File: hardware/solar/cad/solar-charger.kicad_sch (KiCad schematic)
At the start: 20 parts, among them J1 ISENSE_SOLAR, J2 Conn_01x02_Male, J3 ISENSE_DISCHARGE, J4 Conn_01x02_Male, Q1 AOI21357, Q2 AOI21357, Q3 AOI21357, Q4 AOI21357

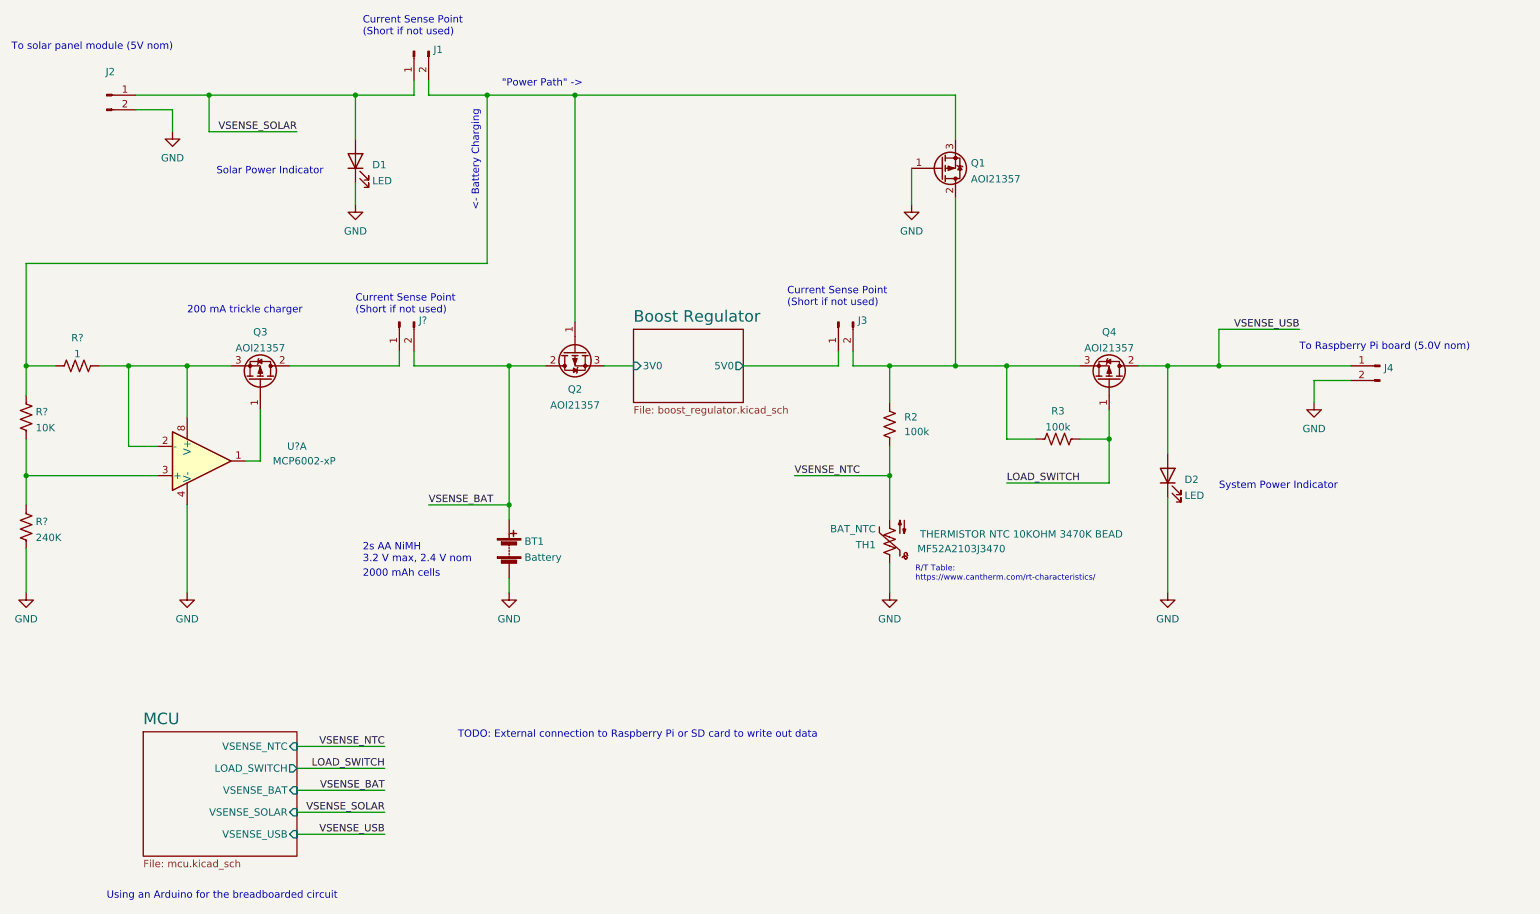
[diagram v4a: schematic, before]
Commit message: Add external I2C connection, LED resistors, op-amp power connections
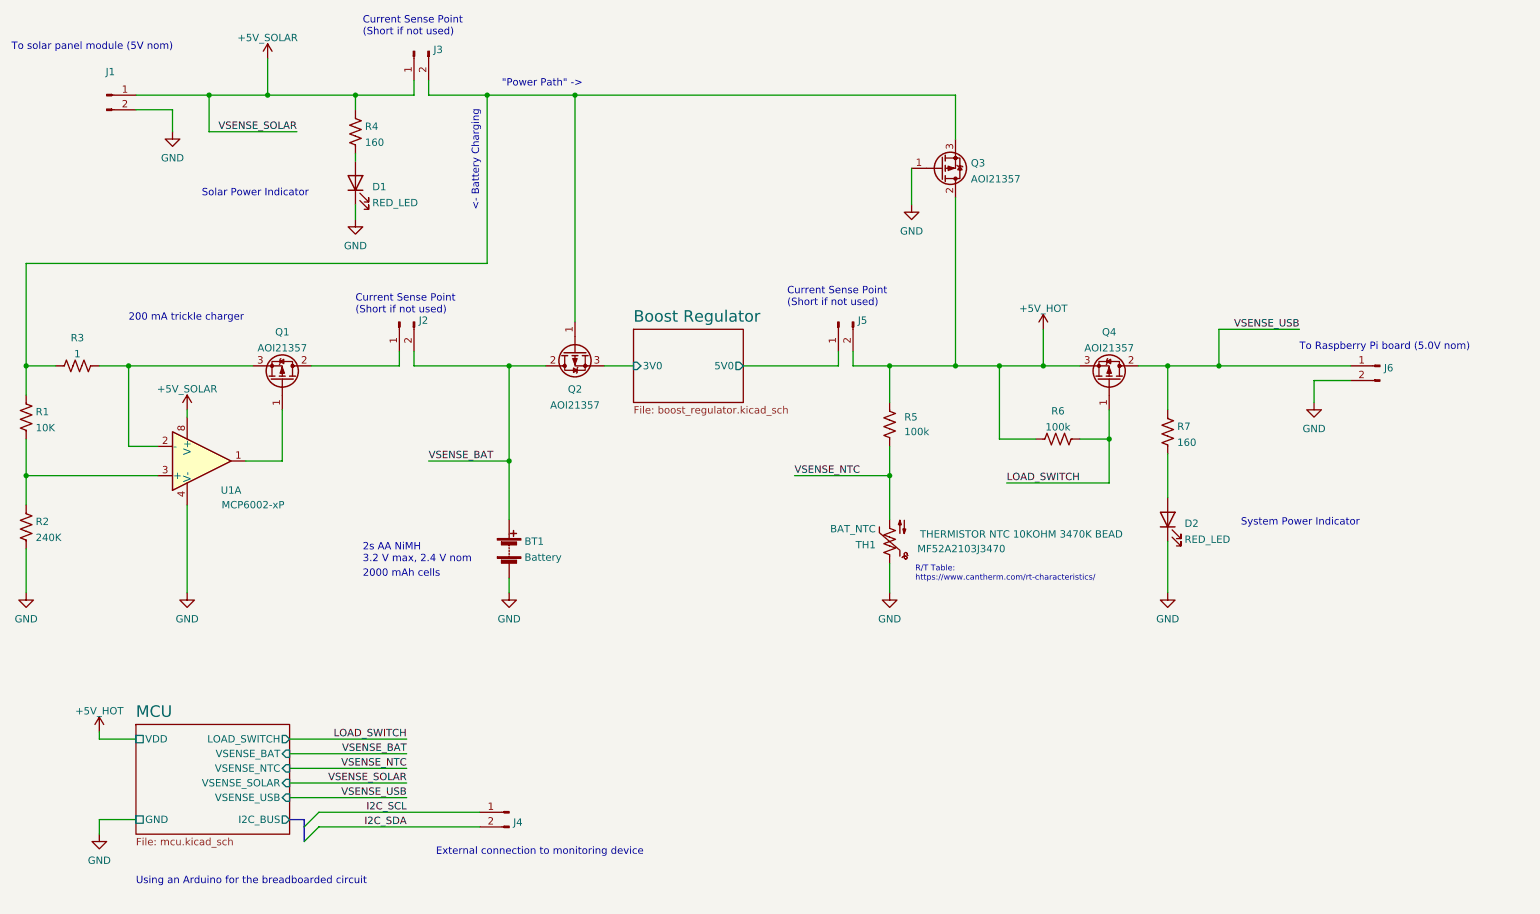
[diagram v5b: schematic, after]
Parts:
- added J4: ISENSE_SOLAR, symbol Connector:Conn_01x02_Male
- added R4, R7: 160, symbol Device:R_US
- D1, D2: value LED -> RED_LED
- gave numbers to parts that had none: 5
- renumbered J2 to J1, J1 to J3, J3 to J5, J4 to J6, Q3 to Q1, Q1 to Q3, R2 to R5, R3 to R6
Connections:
- net VSENSE_USB: now also R7.1; no longer D2.2 (A)
- net at Q1.3 (S), R3.2, U1.2 (-): no longer U1.8 (V+)
- net +5V: now reaches J5.2 (Pin_2), Q3.2 (D), Q4.3 (S), R5.1, R6.1
- net +5V: now also J1.1 (Pin_1), J3.1 (Pin_1), U1.8 (V+), R4.1
- removed net VSENSE_SOLAR: D1.2 (A), J1.1 (Pin_1), J3.1 (Pin_1)
- new net: D1.2 (A), R4.2
- new net: D2.2 (A), R7.2
- new net I2C_SCL: J4.1 (Pin_1)
- new net I2C_SDA: J4.2 (Pin_2)
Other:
- sheet MCU ports: added GND, I2C_BUS, VDD; removed none
- note added: "External connection to monitoring device"
- note removed: "TODO: External connection to Raspberry Pi or SD card to write out data"
- moved on the sheet: D1, D2, Q1

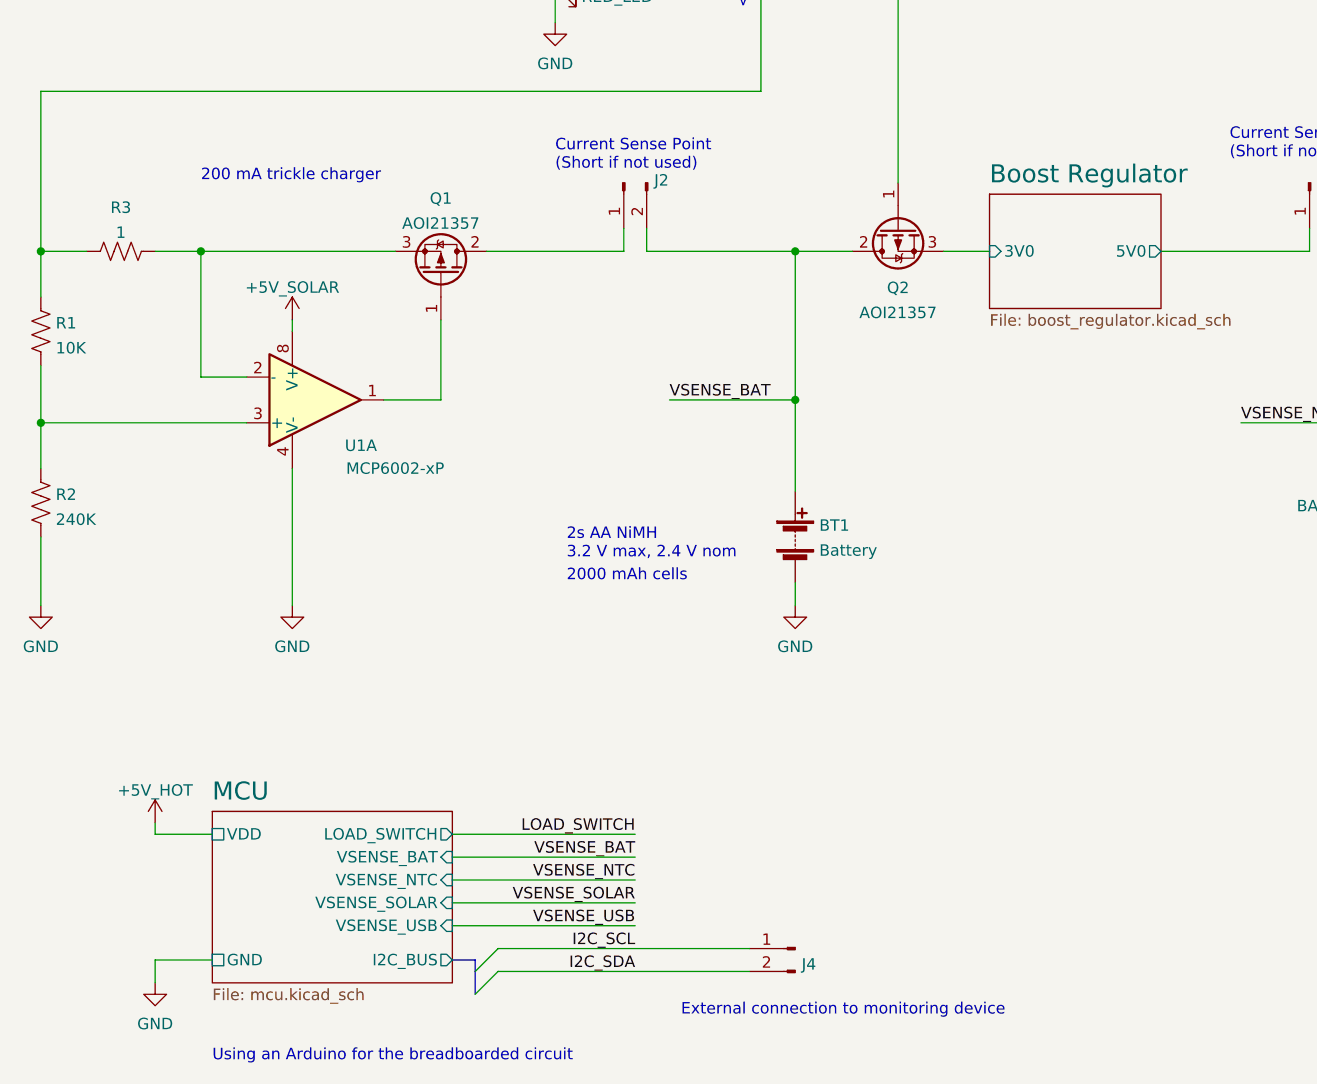
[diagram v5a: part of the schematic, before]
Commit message: add RTC, change charge current based on revised capacity of 1300mAh
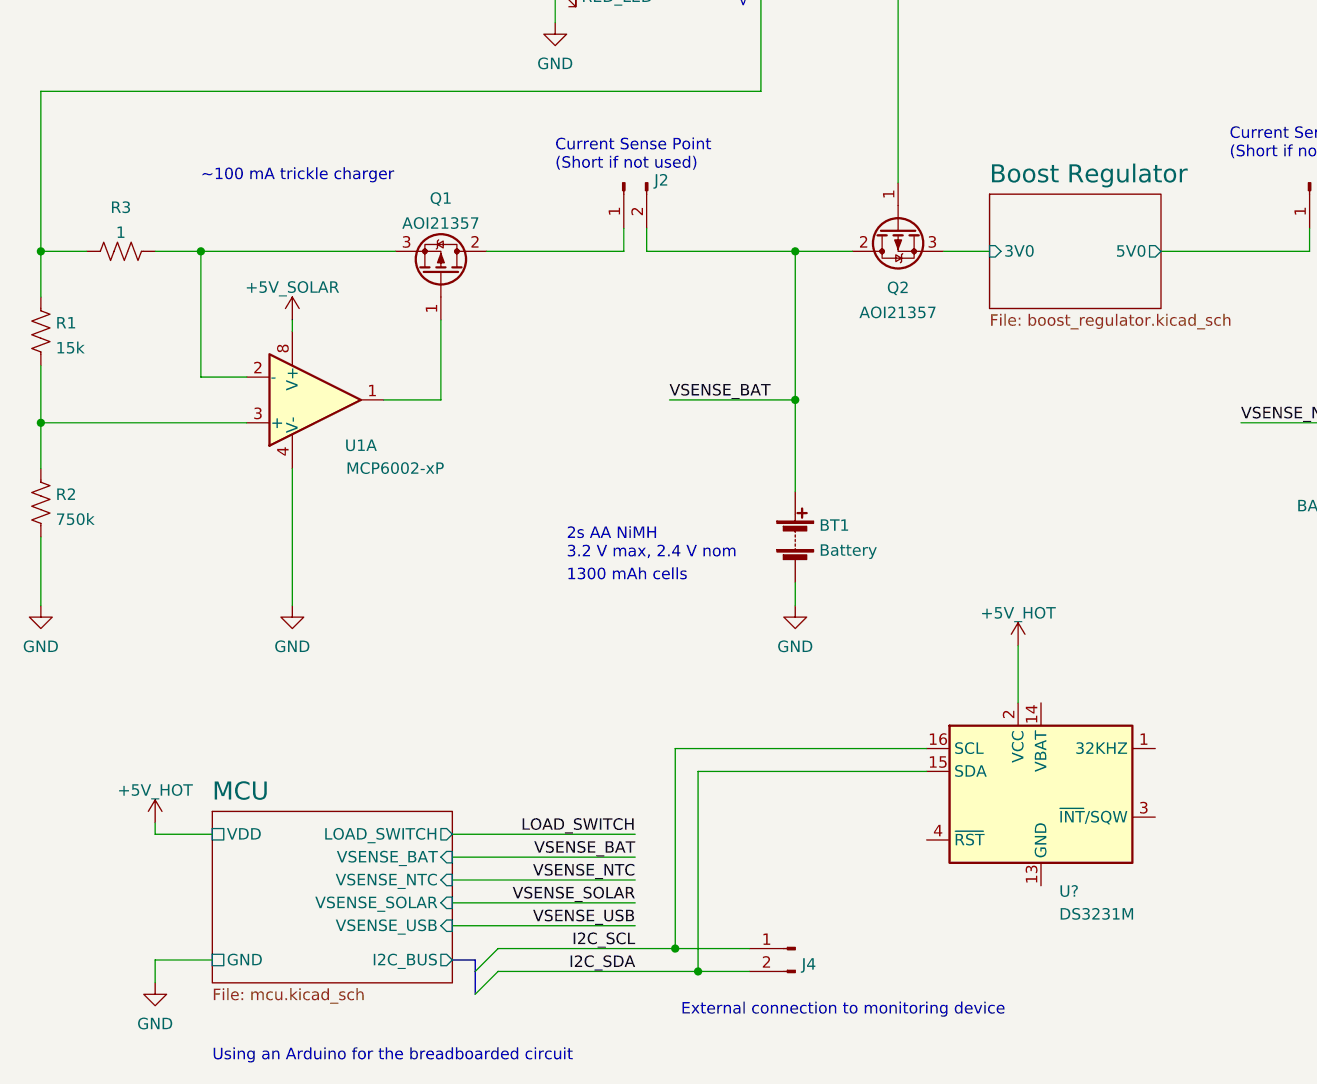
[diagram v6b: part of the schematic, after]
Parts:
- added U?: DS3231M, Package_SO:SOIC-16W_7.5x10.3mm_P1.27mm, symbol Timer_RTC:DS3231M
- R1: value 10K -> 15k
- R2: value 240K -> 750k
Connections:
- net +5V: now also U?.2 (VCC)
- net I2C_SCL: now also U?.16 (SCL)
- net I2C_SDA: now also U?.15 (SDA)
- new net: U?.10 (GND), U?.11 (GND), U?.12 (GND), U?.13 (GND), U?.5 (GND), U?.6 (GND), U?.7 (GND), U?.8 (GND), U?.9 (GND)
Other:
- note added: "1300 mAh cells"
- note added: "~100 mA trickle charger"
- note removed: "200 mA trickle charger"
- note removed: "2000 mAh cells"
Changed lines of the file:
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@@
   (junction (at 232.41 92.71) (diameter 0) (color 0 0 0 0)
   )
+  (junction (at 95.885 170.18) (diameter 0) (color 0 0 0 0)
+  )
   (junction (at 175.26 111.76) (diameter 0) (color 0 0 0 0)
   )
@@
   (junction (at 105.41 45.72) (diameter 0) (color 0 0 0 0)
   )
+  (junction (at 98.425 172.72) (diameter 0) (color 0 0 0 0)
+  )
   (junction (at 186.69 92.71) (diameter 0) (color 0 0 0 0)
   )
@@
     (stroke (width 0) (type default) (color 0 0 0 0))
   )
+  (wire (pts (xy 123.825 150.495) (xy 98.425 150.495))
+    (stroke (width 0) (type default) (color 0 0 0 0))
+  )
   (wire (pts (xy 166.37 92.71) (xy 166.37 90.17))
     (stroke (width 0) (type default) (color 0 0 0 0))
@@
     (stroke (width 0) (type default) (color 0 0 0 0))
   )
+  (wire (pts (xy 98.425 150.495) (xy 98.425 172.72))
+    (stroke (width 0) (type default) (color 0 0 0 0))
+  )
   (wire (pts (xy 38.1 157.48) (xy 44.45 157.48))
     (stroke (width 0) (type default) (color 0 0 0 0))
@@
     (stroke (width 0) (type default) (color 0 0 0 0))
   )
+  (wire (pts (xy 98.425 172.72) (xy 104.14 172.72))
+    (stroke (width 0) (type default) (color 0 0 0 0))
+  )
+  (wire (pts (xy 95.885 170.18) (xy 104.14 170.18))
+    (stroke (width 0) (type default) (color 0 0 0 0))
+  )
   (wire (pts (xy 38.1 156.21) (xy 38.1 157.48))
     (stroke (width 0) (type default) (color 0 0 0 0))
@@
     (stroke (width 0) (type default) (color 0 0 0 0))
   )
+  (wire (pts (xy 133.985 136.525) (xy 133.985 142.875))
+    (stroke (width 0) (type default) (color 0 0 0 0))
+  )
   (wire (pts (xy 223.52 107.95) (xy 223.52 115.57))
     (stroke (width 0) (type default) (color 0 0 0 0))
@@
     (stroke (width 0) (type default) (color 0 0 0 0))
   )
+  (wire (pts (xy 95.885 147.955) (xy 95.885 170.18))
+    (stroke (width 0) (type default) (color 0 0 0 0))
+  )
   (wire (pts (xy 71.12 167.64) (xy 91.44 167.64))
     (stroke (width 0) (type default) (color 0 0 0 0))
@@
     (stroke (width 0) (type default) (color 0 0 0 0))
   )
-  (wire (pts (xy 76.2 172.72) (xy 104.14 172.72))
+  (wire (pts (xy 76.2 172.72) (xy 98.425 172.72))
     (stroke (width 0) (type default) (color 0 0 0 0))
   )
@@
     (stroke (width 0) (type default) (color 0 0 0 0))
   )
+  (wire (pts (xy 123.825 147.955) (xy 95.885 147.955))
+    (stroke (width 0) (type default) (color 0 0 0 0))
+  )
   (wire (pts (xy 149.86 92.71) (xy 166.37 92.71))
     (stroke (width 0) (type default) (color 0 0 0 0))
@@
     (stroke (width 0) (type default) (color 0 0 0 0))
   )
-  (wire (pts (xy 76.2 170.18) (xy 104.14 170.18))
+  (wire (pts (xy 76.2 170.18) (xy 95.885 170.18))
     (stroke (width 0) (type default) (color 0 0 0 0))
   )
@@
     (effects (font (size 1.27 1.27)) (justify left bottom))
   )
-  (text "200 mA trickle charger" (at 43.18 85.09 0)
+  (text "~100 mA trickle charger" (at 43.18 85.09 0)
     (effects (font (size 1.27 1.27)) (justify left bottom))
   )
@@
     (effects (font (size 1.27 1.27)) (justify left bottom))
   )
-  (text "2000 mAh cells" (at 83.82 129.54 0)
+  (text "1300 mAh cells" (at 83.82 129.54 0)
     (effects (font (size 1.27 1.27)) (justify left bottom))
   )
@@
       (effects (font (size 1.27 1.27)) (justify left))
     )
-    (property "Value" "10K" (id 1) (at 27.051 103.4666 0)
+    (property "Value" "15k" (id 1) (at 27.051 103.4666 0)
       (effects (font (size 1.27 1.27)) (justify left))
     )
@@
     (pin "1")
     (pin "2")
+  )
+  (symbol (lib_id "power:+5V_HOT") (at 133.985 136.525 0) (unit 1)
+    (in_bom yes) (on_board yes) (fields_autoplaced)
+    (property "Reference" "#PWR?" (id 0) (at 133.985 140.335 0)
+      (effects (font (size 1.27 1.27)) hide)
+    )
+    (property "Value" "+5V_HOT" (id 1) (at 133.985 132.9205 0))
+    (property "Footprint" "" (id 2) (at 133.985 136.525 0)
+      (effects (font (size 1.27 1.27)) hide)
+    )
+    (property "Datasheet" "" (id 3) (at 133.985 136.525 0)
+      (effects (font (size 1.27 1.27)) hide)
+    )
+    (pin "1")
   )
   (symbol (lib_id "power:GND") (at 109.22 132.08 0) (unit 1)
@@
     (pin "1")
   )
+  (symbol (lib_id "Timer_RTC:DS3231M") (at 136.525 153.035 0) (unit 1)
+    (in_bom yes) (on_board yes) (fields_autoplaced)
+    (property "Reference" "U?" (id 0) (at 138.5444 163.83 0)
+      (effects (font (size 1.27 1.27)) (justify left))
+    )
+    (property "Value" "DS3231M" (id 1) (at 138.5444 166.37 0)
+      (effects (font (size 1.27 1.27)) (justify left))
+    )
+    (property "Footprint" "Package_SO:SOIC-16W_7.5x10.3mm_P1.27mm" (id 2) (at 136.525 168.275 0)
+      (effects (font (size 1.27 1.27)) hide)
+    )
+    (property "Datasheet" "http://datasheets.maximintegrated.com/en/ds/DS3231.pdf" (id 3) (at 143.383 151.765 0)
+      (effects (font (size 1.27 1.27)) hide)
+    )
+    (pin "1")
+    (pin "10")
+    (pin "11")
+    (pin "12")
+    (pin "13")
+    (pin "14")
+    (pin "15")
+    (pin "16")
+    (pin "2")
+    (pin "3")
+    (pin "4")
+    (pin "5")
+    (pin "6")
+    (pin "7")
+    (pin "8")
+    (pin "9")
+  )
   (symbol (lib_id "Connector:Conn_01x02_Male") (at 260.35 92.71 0) (mirror y) (unit 1)
     (in_bom yes) (on_board yes) (fields_autoplaced)
@@
       (effects (font (size 1.27 1.27)) (justify left))
     )
-    (property "Value" "240K" (id 1) (at 27.051 122.5166 0)
+    (property "Value" "750k" (id 1) (at 27.051 122.5166 0)
       (effects (font (size 1.27 1.27)) (justify left))
     )
@@
       (reference "#PWR?") (unit 1) (value "+5V_SOLAR") (footprint "")
     )
+    (path "/7c656cfc-f7dd-4798-9e06-b1a5d19e212a"
+      (reference "#PWR?") (unit 1) (value "+5V_HOT") (footprint "")
+    )
     (path "/a7f620a7-01fc-4eed-a181-4d7e6b70f52a"
       (reference "#PWR?") (unit 1) (value "+5V_SOLAR") (footprint "")
@@
     )
     (path "/27c6cc50-ac41-453f-8f74-90611a703dbb"
-      (reference "R1") (unit 1) (value "10K") (footprint "")
+      (reference "R1") (unit 1) (value "15k") (footprint "")
     )
     (path "/f1c4192e-738f-41d6-a0ec-8dd6c1776085"
-      (reference "R2") (unit 1) (value "240K") (footprint "")
+      (reference "R2") (unit 1) (value "750k") (footprint "")
     )
     (path "/d93616ba-c995-4ea9-9de7-28676c40ec2b"
@@
       (reference "U1") (unit 3) (value "MCP6002-xP") (footprint "")
     )
-  )
+    (path "/ec6b684a-ac78-42b3-962f-04161b59563a"
+      (reference "U?") (unit 1) (value "DS3231M") (footprint "Package_SO:SOIC-16W_7.5x10.3mm_P1.27mm")
+    )
+  )
